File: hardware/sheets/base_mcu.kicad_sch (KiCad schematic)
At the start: 22 parts, among them J1 DevKit J1 (left row), J2 DevKit J3 (right row), J4 Qwiic, J5 Expansion 2x10

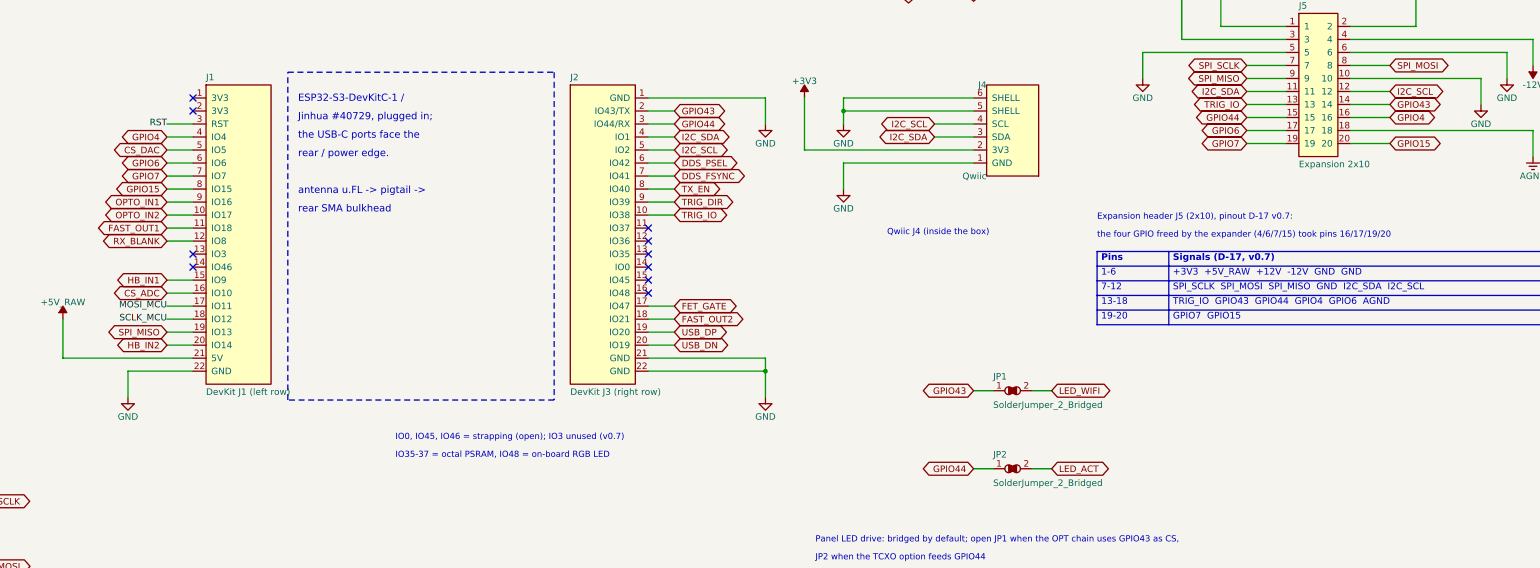
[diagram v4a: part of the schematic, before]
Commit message: Boards as hand-reworked by the instructor 2026-09-18 (Decision #66): three 2x20 links re-placed, jumpers -> headers, TCXO removed, 16 SMA; layout and routing in progress; review in the course repo notes
Co-Authored-By: Claude Fable 5.1 <noreply@anthropic.com>
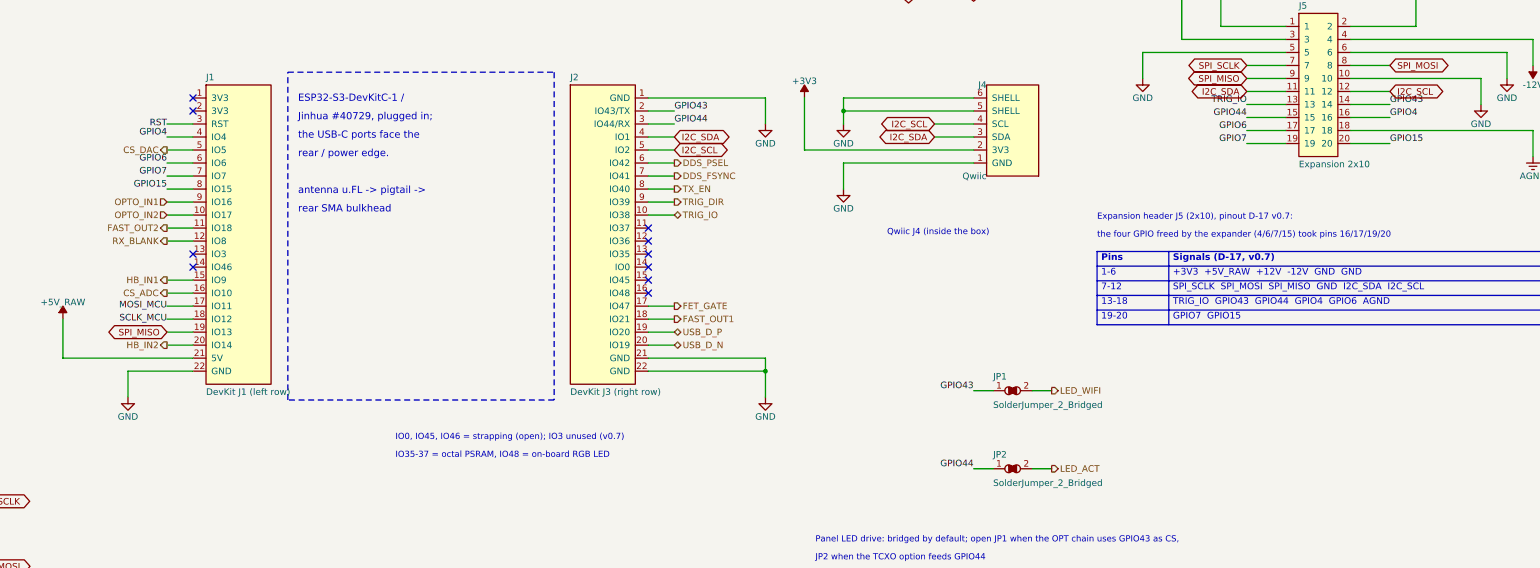
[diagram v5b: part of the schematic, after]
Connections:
- net FAST_OUT1: now also J2.18 (IO21); no longer J1.11 (IO18)
- net FAST_OUT2: now also J1.11 (IO18); no longer J2.18 (IO21)
- net USB_DN renamed USB_D_N
- net USB_DP renamed USB_D_P

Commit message: WIP main board routing + schematic (instructor), 2026-09-21 05:04
Co-Authored-By: Claude Fable 5.1 <noreply@anthropic.com>
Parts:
- removed JP1, JP2: SolderJumper_2_Bridged, class_board:SolderJumper-2_P1.3mm_Bridged_RoundedPad1.0x1.5mm, symbol class_board:SolderJumper_2_Bridged
- removed NT1: AGND-GND star, class_board:NetTie-2_SMD_Pad2.0mm, symbol class_board:NetTie_2
- added R717, R718, R719: 0, Resistor_SMD:R_0805_2012Metric_Pad1.20x1.40mm_HandSolder, symbol class_board:R0603_100
- TP1: value TP -> RST
- TP2: value TP -> GND
- TP3: value TP -> +3V3
- TP4: value TP -> +5V
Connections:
- net AGND: now also R719.1
- net GND: now also R719.2
- net GPIO43: now also R717.1
- net GPIO44: now also R718.1
- net LED_ACT: now also R718.2
- net LED_WIFI: now also R717.2

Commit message: hardware: board, sheets and DC jack footprint as on disk 2026-09-27 (snapshot committed by the projector-developer session, Shayne 2026-09-27)
Co-Authored-By: Claude Fable 5.1 <noreply@anthropic.com>
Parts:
- removed J4: Qwiic, class_board:CONN-SMD_4P-P1.00_XY-SM04B-SRSS-TB, symbol class_board:QWIIC_SM04B-SRSS
- removed J5: Expansion 2x10, Connector_PinHeader_2.54mm:PinHeader_2x10_P2.54mm_Vertical, symbol class_board:HDR_2x10_MALE
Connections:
- net GPIO15: no longer names the net of J1.8 (IO15)
- net GPIO4: no longer names the net of J1.4 (IO4)
- net GPIO6: no longer names the net of J1.6 (IO6)
- net GPIO7: no longer names the net of J1.7 (IO7)
- no-connect marks 10 -> 14
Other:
- note added: "GPIO15"
- note added: "GPIO4"
- note added: "GPIO6"
- note added: "GPIO7"
- note removed: "+3V3 +5V_RAW +12V -12V GND GND"
- note removed: "1-6"
- note removed: "13-18"
- note removed: "19-20"
- note removed: "7-12"
- note removed: "Expansion header J5 (2x10), pinout D-17 v0.7:"
- note removed: "GPIO7 GPIO15"
- note removed: "Pins"
- note removed: "Qwiic J4 (inside the box)"
- note removed: "SPI_SCLK SPI_MOSI SPI_MISO GND I2C_SDA I2C_SCL"
- note removed: "Signals (D-17, v0.7)"
- note removed: "TRIG_IO GPIO43 GPIO44 GPIO4 GPIO6 AGND"
- note removed: "the four GPIO freed by the expander (4/6/7/15) took pins 16/17/19/20"

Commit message: hardware: instructor 2026-10-01 saves synced (one GND net on both boards, PCB updated, R951-R958, headers DNP per Decision #73) + nmr_tx R808 -> TX_VMID, C813 removed, R805/R806 10 k (review B2)
Co-Authored-By: Claude Fable 5.1 <noreply@anthropic.com>
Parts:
- removed R719: 0, Resistor_SMD:R_0805_2012Metric_Pad1.20x1.40mm_HandSolder, symbol class_board:R0603_100
- J1, J2: now not fitted; now left out of the parts list
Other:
- note removed: "Placed at the B1/BASE boundary."
- note removed: "The ONLY AGND-GND join (net tie NT1, copper only)."
